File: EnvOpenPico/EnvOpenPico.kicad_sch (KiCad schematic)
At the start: 61 parts, among them J2 SKRKAEE020, J3 2.54mm header 01x20, J4 2.54mm header 01x20, J5 Conn_01x03_Male, Q1 Si2329DS, U1 TLV75533PDBVR, U2 24LC256, U3 RP2040, Y1 3225_4P

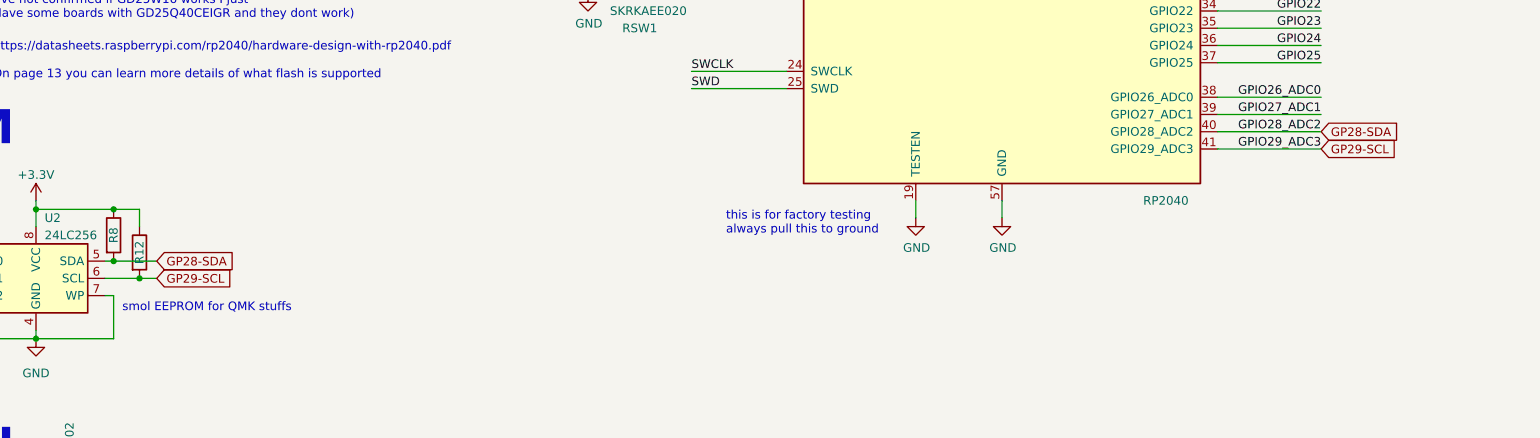
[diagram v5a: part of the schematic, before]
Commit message: removed some parts and swapped flash to soic package for stock reasons.
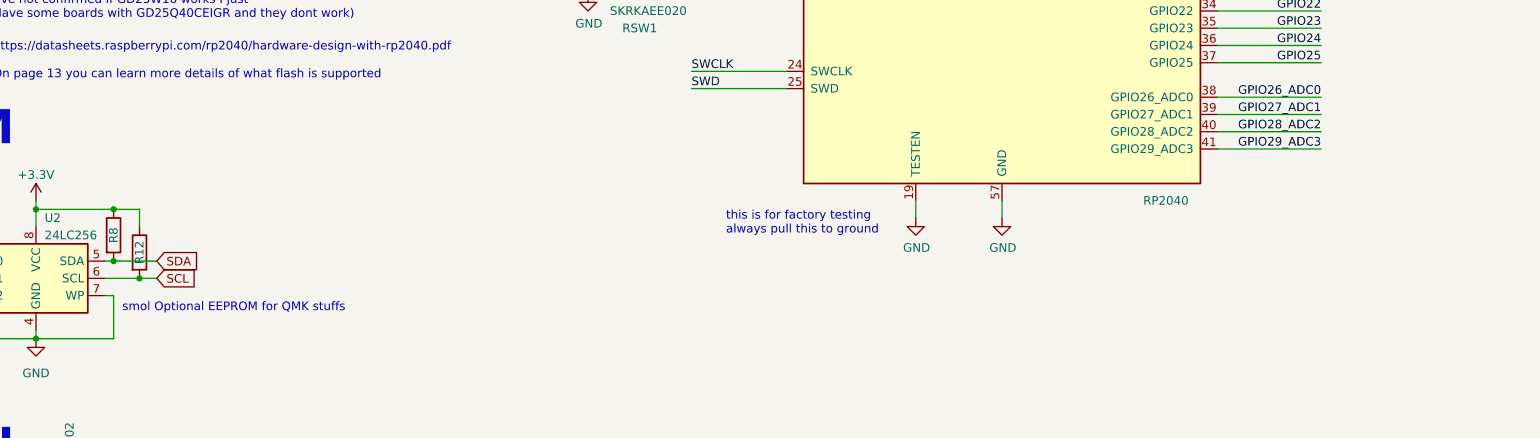
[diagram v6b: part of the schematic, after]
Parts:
- FLASH1: footprint Package_SON:SON-8-1EP_3x2mm_P0.5mm_EP1.4x1.6mm -> Package_SO:SO-8_3.9x4.9mm_P1.27mm
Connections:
- net GP28-SDA renamed GPIO28_ADC2
- net GPIO28_ADC2: no longer R8.2, U2.5 (SDA)
- net GP29-SCL renamed SCL
- net SCL: no longer U3.41 (GPIO29_ADC3)
- new net GPIO29_ADC3: U3.41 (GPIO29_ADC3)
- new net SDA: R8.2, U2.5 (SDA)
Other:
- note added: "smol Optional EEPROM for QMK stuffs"
- note removed: "smol EEPROM for QMK stuffs"
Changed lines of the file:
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@@
     (effects (font (size 1.27 1.27)) (justify left bottom))
   )
-  (text "smol EEPROM for QMK stuffs" (at 68.58 212.09 0)
+  (text "smol Optional EEPROM for QMK stuffs" (at 68.58 212.09 0)
     (effects (font (size 1.27 1.27)) (justify left bottom))
   )
@@
     )
   )
-  (global_label "GP29-SCL" (shape input) (at 73.66 207.01 0) (fields_autoplaced)
+  (global_label "SCL" (shape input) (at 73.66 207.01 0) (fields_autoplaced)
     (effects (font (size 1.27 1.27)) (justify left))
-    (property "Intersheet References" "${INTERSHEET_REFS}" (id 0) (at 86.0232 206.9306 0)
-      (effects (font (size 1.27 1.27)) (justify left) hide)
-    )
-  )
-  (global_label "GP29-SCL" (shape input) (at 245.11 187.96 0) (fields_autoplaced)
-    (effects (font (size 1.27 1.27)) (justify left))
-    (property "Intersheet References" "${INTERSHEET_REFS}" (id 0) (at 257.4732 187.8806 0)
+    (property "Intersheet References" "${INTERSHEET_REFS}" (id 0) (at 79.4918 206.9306 0)
       (effects (font (size 1.27 1.27)) (justify left) hide)
     )
@@
     )
   )
-  (global_label "GP28-SDA" (shape input) (at 73.66 204.47 0) (fields_autoplaced)
+  (global_label "SDA" (shape input) (at 73.66 204.47 0) (fields_autoplaced)
     (effects (font (size 1.27 1.27)) (justify left))
-    (property "Intersheet References" "${INTERSHEET_REFS}" (id 0) (at 86.0837 204.3906 0)
+    (property "Intersheet References" "${INTERSHEET_REFS}" (id 0) (at 79.5523 204.3906 0)
       (effects (font (size 1.27 1.27)) (justify left) hide)
     )
@@
     (property "Intersheet References" "${INTERSHEET_REFS}" (id 0) (at 0 0 0)
       (effects (font (size 1.27 1.27)) hide)
-    )
-  )
-  (global_label "GP28-SDA" (shape input) (at 245.11 185.42 0) (fields_autoplaced)
-    (effects (font (size 1.27 1.27)) (justify left))
-    (property "Intersheet References" "${INTERSHEET_REFS}" (id 0) (at 257.5337 185.3406 0)
-      (effects (font (size 1.27 1.27)) (justify left) hide)
     )
   )
@@
     (property "Reference" "FLASH1" (id 0) (at 78.74 133.35 0))
     (property "Value" "W25Q16JVUXIQ" (id 1) (at 78.74 146.05 0))
-    (property "Footprint" "Package_SON:SON-8-1EP_3x2mm_P0.5mm_EP1.4x1.6mm" (id 2) (at 78.74 133.35 0)
+    (property "Footprint" "Package_SO:SO-8_3.9x4.9mm_P1.27mm" (id 2) (at 78.74 133.35 0)
       (effects (font (size 1.27 1.27)) (justify left bottom) hide)
     )
@@
     )
     (path "/00000000-0000-0000-0000-0000608edada"
-      (reference "FLASH1") (unit 1) (value "W25Q16JVUXIQ") (footprint "Package_SON:SON-8-1EP_3x2mm_P0.5mm_EP1.4x1.6mm")
+      (reference "FLASH1") (unit 1) (value "W25Q16JVUXIQ") (footprint "Package_SO:SO-8_3.9x4.9mm_P1.27mm")
     )
     (path "/00000000-0000-0000-0000-000061cdafdc"

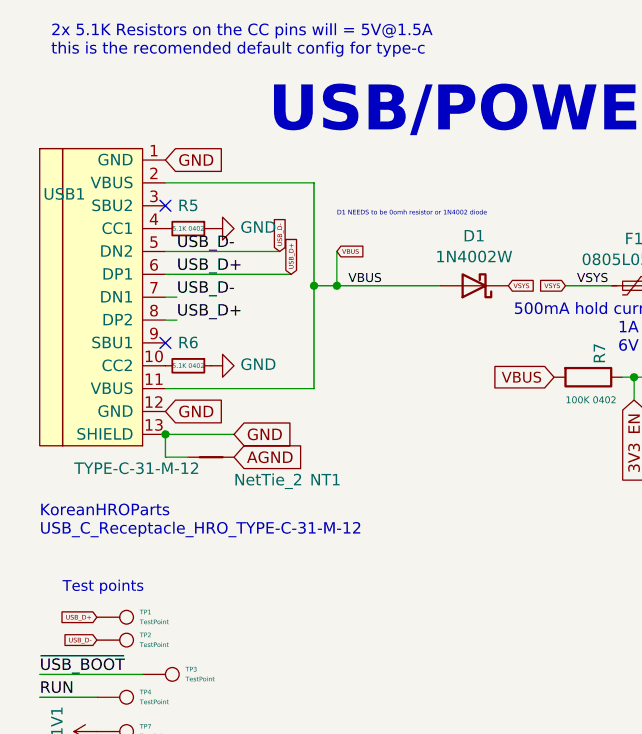
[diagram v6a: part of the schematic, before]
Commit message: made some changes in the schematic to conform more with the USB Spec,
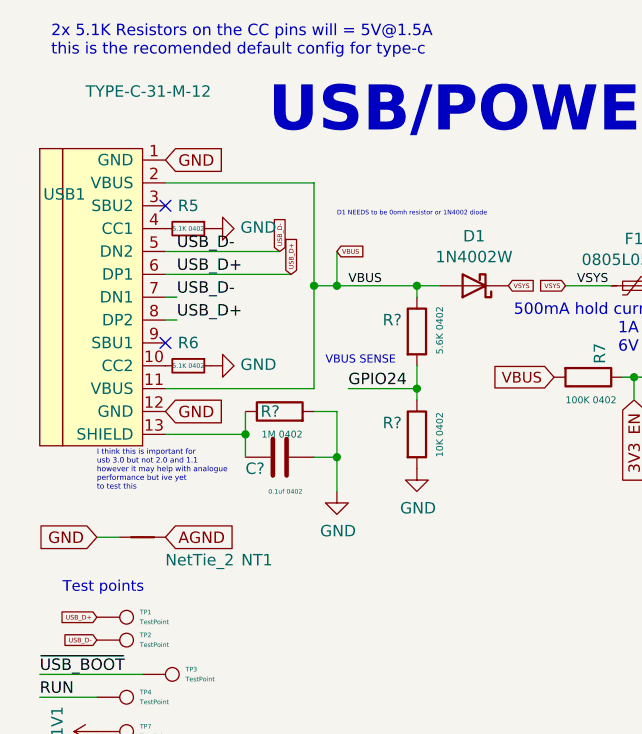
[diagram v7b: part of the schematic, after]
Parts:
- added C?: 0.1uf 0402, Capacitor_SMD:C_0402_1005Metric, symbol Device:C
- added R?: 1M 0402, Resistor_SMD:R_0402_1005Metric, symbol Device:R
- added R?: 10K 0402, Resistor_SMD:R_0402_1005Metric, symbol Device:R
- added R?: 5.6K 0402, Resistor_SMD:R_0402_1005Metric, symbol Device:R
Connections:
- net GND: now also C?.1, R?.2, R?.2; no longer USB1.13 (SHIELD)
- net GPIO24: now also R?.1, R?.2
- net VBUS: now also R?.1
- new net: C?.2, R?.1, USB1.13 (SHIELD)
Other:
- note added: "I think this is important for usb 3.0 but not 2.0 and 1.1 however it may help with analogue performance but ive yet to test this"
- note added: "VBUS SENSE"
- note removed: "KoreanHROParts USB_C_Receptacle_HRO_TYPE-C-31-M-12"
- moved on the sheet: NT1
